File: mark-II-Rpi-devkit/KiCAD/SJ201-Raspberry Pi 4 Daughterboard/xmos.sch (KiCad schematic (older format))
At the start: 55 parts, among them J10 Debug Connector, J8 MIC, Q4 FDV301N, U10 SPK0838HT4H-1, U11 SPK0838HT4H-1, U12 NCP303LSN09, U5 SN74LVC125APWR, U8 XMOS-XVF3510, U9 AT25SF161 16MBIT, X1 SG-210STF 24M

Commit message: SJ201 - Removed CM108b soundcard, added in I2S to Line out, ATTin402. Moved holes in layout. SJ202 - extened length to plug into USB2.0 port
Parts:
- removed R9: 4.7k, Resistor_SMD:R_0402_1005Metric, symbol Device:R_Small
- removed TP28: TestPoint, TestPoint:TestPoint_Pad_D2.0mm, symbol Connector:TestPoint
- C55, C56: MPN CC0402KRX5R6BB105 -> CL05A105KA5NQNC; SKU 302010040 -> (none)
- C65: Link (none) -> https://lcsc.com/product-detail/Multilayer-Ceramic-Capacito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; MPN CC0402KRX7R9BB222 -> 0402B222K500NT; SKU 302010022 -> (none); Vendor (none) -> LCSC
- J10: MPN (none) -> DNP
- J8: LCSC C191721 -> (none); MPN (none) -> DNP
- PWR2: value LED -> LED_RED
- Q4: value FDV301N -> 2N7002; Category Discrete Semiconductor Products -> (none); DK_Datasheet_Link https://media.digikey.com/pdf/Data%20Sheets/Fairchild%20PDF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 -> (none); DK_Detail_Page /product-detail/en/on-semiconductor/FDV301N/FDV301NCT-ND/45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 -> (none); Description MOSFET N-CH 25V 220MA SOT-23 -> MOSFET N TRENCH 60V 115MA 2.5V @ 250UA 7.5 ? @ 500MA,10V SO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; Digi-Key_PN FDV301NCT-ND -> (none); Family Transistors - FETs, MOSFETs - Single -> (none); LCSC C15310 -> C8545; MPN FDV301N -> 2N7002; Manufacturer ON Semiconductor -> (none); Status Active -> (none)
- R34: MPN (none) -> 0402WGF330JTCE
- R5: MPN (none) -> 0402WGF100JTCE
- U10, U11: value SPK0838HT4H-1 -> SPK0641HT4H-1; Digikey 423-1432-1-ND -> 423-1425-1-ND; Link https://www.digikey.com/product-detail/en/knowles/SPK0838HT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 -> https://www.digikey.com/product-detail/en/knowles/SPK0641HT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; MPN SPK0838HT4H-1 -> SPK0641HT4H-1
- U8: MPN XVF3510 -> XVF3510-QF60-C
- U9: MPN AT25SF161 16MBIT -> AT25SF161-SSHD-T
- X1: MPN SG-210STF 24M -> SG-210STF 24.0000ML3
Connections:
- net labels added: GPIO22, GPIO23, GPIO24, GPIO25, SCL_XMOS, SDA_XMOS
- net labels removed: I2C_SCL, I2C_SDA, INT_N, TP5
- wire segments 237 -> 239
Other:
- note added: "Optional Mic:\nSPK0838HT4H-1"
- note removed: "Optional Mic:\nIM69D130"

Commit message: SJ-201 v3, sent to PCB Fab. Removed USB Hub, add in I2S to Line Out
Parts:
- added J15: Output, Connector_PinHeader_1.27mm:PinHeader_1x04_P1.27mm_Vertical_SMD_Pin1Left, symbol Connector_Generic:Conn_01x04
- added R58, R59, R60, R61: 0R DNP, Resistor_SMD:R_0603_1608Metric, symbol Device:R_Small
- C65: Tempo (none) -> C0402C222K5RACTU
- PWR2: Tempo (none) -> 19-217/R6C-AL1M2VY/3T
- Q4: Description MOSFET N TRENCH 60V 115MA 2.5V @ 250UA 7.5 ? @ 500MA,10V SO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 -> N-Channel MOSFET, Enhancement Mode, 60V, 0.115A, 7.5Ω; Manufacturer (none) -> ON Semiconductor
- R32, R34, R35, R36: Tempo (none) -> RC0402FR-0733RL
- R41: Tempo (none) -> RC0402JR-074K7L
- R43, R44, R45, R46: Tempo (none) -> RC0402FR-07100RL
- R5: Tempo (none) -> ERJ-2RKF10R0X
- U9: Digikey 1265-1230-1-ND -> 1265-1278-2-ND; Link https://www.digikey.com/product-detail/en/adesto-technologi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 -> https://www.digikey.com/en/products/detail/adesto-technolog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; MPN AT25SF161-SSHD-T -> AT25SF161-SHD-T
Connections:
- wire segments 239 -> 243
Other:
- note added: "I2S Data out \nfrom XMOS to\nI2S to Lineout IC"
- note removed: "I2S Data from \nUSB Soundcard"
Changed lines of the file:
@@
 Sheet 6 6
 Title ""
-Date "2020-09-26"
-Rev "0.67b"
+Date "2020-10-02"
+Rev "0.67c"
 Comp ""
 Comment1 ""
@@
 F 4 "C25105" H 2150 5150 50  0001 C CNN "LCSC"
 F 5 "0402WGF330JTCE" H 2150 5150 50  0001 C CNN "MPN"
+F 6 "RC0402FR-0733RL" H 2150 5150 50  0001 C CNN "Tempo"
 	1    2150 5150
 	1    0    0    -1
@@
 F 4 "0402WGF330JTCE" H 2225 4350 50  0001 C CNN "MPN"
 F 5 "C25105" H 2225 4350 50  0001 C CNN "LCSC"
+F 6 "RC0402FR-0733RL" H 2225 4350 50  0001 C CNN "Tempo"
 	1    2225 4350
 	0    1    1    0
@@
 F 4 "0402WGF330JTCE" H 2225 4250 50  0001 C CNN "MPN"
 F 5 "C25105" H 2225 4250 50  0001 C CNN "LCSC"
+F 6 "RC0402FR-0733RL" H 2225 4250 50  0001 C CNN "Tempo"
 	1    2225 4250
 	0    1    1    0
@@
 F 4 "0402WGF330JTCE" H 1550 3250 50  0001 C CNN "MPN"
 F 5 "C25105" H 1550 3250 50  0001 C CNN "LCSC"
+F 6 "RC0402FR-0733RL" H 1550 3250 50  0001 C CNN "Tempo"
 	1    1550 3250
 	0    1    1    0
@@
 F 2 "Package_SO:SOIC-8_5.23x5.23mm_P1.27mm" H 7200 2025 50  0001 C CNN
 F 3 "http://ww1.microchip.com/downloads/en/DeviceDoc/Atmel-8707-SEEPROM-AT25010B-020B-040B-Datasheet.pdf" H 7200 2025 50  0001 C CNN
-F 4 "1265-1230-1-ND" H 7200 2025 50  0001 C CNN "Digikey"
-F 5 "AT25SF161-SSHD-T" H 7200 2025 50  0001 C CNN "MPN"
-F 6 "https://www.digikey.com/product-detail/en/adesto-technologies/AT25SF161-SSHD-T/1265-1230-2-ND/6124893" H 7200 2025 50  0001 C CNN "Link"
+F 4 "1265-1278-2-ND" H 7200 2025 50  0001 C CNN "Digikey"
+F 5 "AT25SF161-SHD-T" H 7200 2025 50  0001 C CNN "MPN"
+F 6 "https://www.digikey.com/en/products/detail/adesto-technologies/AT25SF161-SHD-T/6827526" H 7200 2025 50  0001 C CNN "Link"
 F 7 "C93710" H 7200 2025 50  0001 C CNN "LCSC"
 	1    7200 2025
@@
 F 4 "0402WGF4701TCE" H 5125 3450 50  0001 C CNN "MPN"
 F 5 "C25900" H 5125 3450 50  0001 C CNN "LCSC"
+F 6 "RC0402JR-074K7L" H 5125 3450 50  0001 C CNN "Tempo"
 	1    5125 3450
 	-1   0    0    1
@@
 F 4 "0402WGF1000TCE" H 10200 3600 50  0001 C CNN "MPN"
 F 5 "C25076" H 10200 3600 50  0001 C CNN "LCSC"
+F 6 "RC0402FR-07100RL" H 10200 3600 50  0001 C CNN "Tempo"
 	1    10200 3600
 	0    1    1    0
@@
 F 4 "0402WGF1000TCE" H 10200 3700 50  0001 C CNN "MPN"
 F 5 "C25076" H 10200 3700 50  0001 C CNN "LCSC"
+F 6 "RC0402FR-07100RL" H 10200 3700 50  0001 C CNN "Tempo"
 	1    10200 3700
 	0    1    1    0
@@
 F 4 "0402WGF1000TCE" H 10200 4925 50  0001 C CNN "MPN"
 F 5 "C25076" H 10200 4925 50  0001 C CNN "LCSC"
+F 6 "RC0402FR-07100RL" H 10200 4925 50  0001 C CNN "Tempo"
 	1    10200 4925
 	0    1    1    0
@@
 F 4 "0402WGF1000TCE" H 10200 5025 50  0001 C CNN "MPN"
 F 5 "C25076" H 10200 5025 50  0001 C CNN "LCSC"
+F 6 "RC0402FR-07100RL" H 10200 5025 50  0001 C CNN "Tempo"
 	1    10200 5025
 	0    1    1    0
@@
 Text GLabel 4025 1550 2    51   Input ~ 0
 I2S_DATA
-Text Notes 5050 1175 0    63   ~ 0
-I2S Data from \nUSB Soundcard
 $Comp
 L kevin:Ferrite_Bead_Small FB6
@@
 F 8 "" H 3675 8275 60  0001 L CNN "DK_Datasheet_Link"
 F 9 "" H 3675 8375 60  0001 L CNN "DK_Detail_Page"
-F 10 "MOSFET N TRENCH 60V 115MA 2.5V @ 250UA 7.5 ? @ 500MA,10V SOT-23(SOT-23-3) ROHS" H 3675 8475 60  0001 L CNN "Description"
-F 11 "" H 3675 8575 60  0001 L CNN "Manufacturer"
+F 10 "N-Channel MOSFET, Enhancement Mode, 60V, 0.115A, 7.5Ω" H 3675 8475 60  0001 L CNN "Description"
+F 11 "ON Semiconductor" H 3675 8575 60  0001 L CNN "Manufacturer"
 F 12 "" H 3675 8675 60  0001 L CNN "Status"
 F 13 "C8545" H 3475 7475 50  0001 C CNN "LCSC"
@@
 F 6 "https://lcsc.com/product-detail/Others_TOGIALED-TJ-S1608SW6TGLC2R-A5_C192315.html" V 3325 7075 50  0001 C CNN "Link"
 F 7 "304090042" H 3325 7075 50  0001 C CNN "SKU"
+F 8 "19-217/R6C-AL1M2VY/3T" H 3325 7075 50  0001 C CNN "Tempo"
 	1    3325 7075
 	-1   0    0    1
@@
 F 4 "C25077" H 2150 5350 50  0001 C CNN "LCSC"
 F 5 "0402WGF100JTCE" H 2150 5350 50  0001 C CNN "MPN"
+F 6 "ERJ-2RKF10R0X" H 2150 5350 50  0001 C CNN "Tempo"
 	1    2150 5350
 	1    0    0    -1
@@
 F 6 "https://lcsc.com/product-detail/Multilayer-Ceramic-Capacitors-MLCC-SMD-SMT_2-2nF-222-10-50V_C1531.html/?href=jlc-SMT" H 1050 7500 50  0001 C CNN "Link"
 F 7 "LCSC" H 1050 7500 50  0001 C CNN "Vendor"
+F 8 "C0402C222K5RACTU" H 1050 7500 50  0001 C CNN "Tempo"
 	1    1050 7500
 	1    0    0    -1
@@
 Wire Wire Line
 	4025 4500 4225 4500
-Text GLabel 4225 4500 2    51   Input ~ 0
+Text GLabel 4975 4500 2    51   Input ~ 0
 GPIO22
-Text GLabel 4225 4700 2    51   Input ~ 0
+Text GLabel 4975 4700 2    51   Input ~ 0
 GPIO24
-Text GLabel 4225 4800 2    51   Input ~ 0
+Text GLabel 4975 4800 2    51   Input ~ 0
 GPIO25
-Text GLabel 4225 4600 2    51   Input ~ 0
+Text GLabel 4975 4600 2    51   Input ~ 0
 GPIO23
 Wire Wire Line
@@
 Wire Wire Line
 	4025 3050 4725 3050
+$Comp
+L Connector_Generic:Conn_01x04 J15
+U 1 1 5F75C2D9
+P 4775 5125
+F 0 "J15" H 4775 5350 50  0000 C CNN
+F 1 "Output" H 4775 4825 50  0000 C CNN
+F 2 "Connector_PinHeader_1.27mm:PinHeader_1x04_P1.27mm_Vertical_SMD_Pin1Left" H 4775 5125 50  0001 C CNN
+F 3 "~" H 4775 5125 50  0001 C CNN
+F 4 "DNP" H 4775 5125 50  0001 C CNN "MPN"
+	1    4775 5125
+	-1   0    0    -1
+$EndComp
+Text GLabel 4975 5025 2    51   Input ~ 0
+TP1
+Text GLabel 4975 5125 2    51   Input ~ 0
+TP2
+Text GLabel 4975 5225 2    51   Input ~ 0
+TP3
+Text GLabel 4975 5325 2    51   Input ~ 0
+TP4
+Text Notes 4650 1700 0    63   ~ 0
+I2S Data out \nfrom XMOS to\nI2S to Lineout IC
+$Comp
+L Device:R_Small R?
+U 1 1 5F9B65AF
+P 4325 4500
+AR Path="/5EA9C461/5F9B65AF" Ref="R?"  Part="1"
+AR Path="/5EA9C67D/5F9B65AF" Ref="R?"  Part="1"
+AR Path="/5EA9C76D/5F9B65AF" Ref="R58"  Part="1"
+F 0 "R58" V 4275 4275 50  0000 L CNN
+F 1 "0R DNP" V 4375 4600 50  0000 L CNN
+F 2 "Resistor_SMD:R_0603_1608Metric" H 4325 4500 50  0001 C CNN
+F 3 "~" H 4325 4500 50  0001 C CNN
+F 4 "DNP-0603WAF0000T5E" H 4325 4500 50  0001 C CNN "MPN"
+F 5 "C21189-DNP" H 4325 4500 50  0001 C CNN "LCSC"
+	1    4325 4500
+	0    1    1    0
+$EndComp
+$Comp
+L Device:R_Small R?
+U 1 1 5F9E9135
+P 4325 4600
+AR Path="/5EA9C461/5F9E9135" Ref="R?"  Part="1"
+AR Path="/5EA9C67D/5F9E9135" Ref="R?"  Part="1"
+AR Path="/5EA9C76D/5F9E9135" Ref="R59"  Part="1"
+F 0 "R59" V 4275 4375 50  0000 L CNN
+F 1 "0R DNP" V 4375 4700 50  0000 L CNN
+F 2 "Resistor_SMD:R_0603_1608Metric" H 4325 4600 50  0001 C CNN
+F 3 "~" H 4325 4600 50  0001 C CNN
+F 4 "DNP-0603WAF0000T5E" H 4325 4600 50  0001 C CNN "MPN"
+F 5 "C21189-DNP" H 4325 4600 50  0001 C CNN "LCSC"
+	1    4325 4600
+	0    1    1    0
+$EndComp
+$Comp
+L Device:R_Small R?
+U 1 1 5F9E932A
+P 4325 4700
+AR Path="/5EA9C461/5F9E932A" Ref="R?"  Part="1"
+AR Path="/5EA9C67D/5F9E932A" Ref="R?"  Part="1"
+AR Path="/5EA9C76D/5F9E932A" Ref="R60"  Part="1"
+F 0 "R60" V 4275 4475 50  0000 L CNN
+F 1 "0R DNP" V 4375 4800 50  0000 L CNN
+F 2 "Resistor_SMD:R_0603_1608Metric" H 4325 4700 50  0001 C CNN
+F 3 "~" H 4325 4700 50  0001 C CNN
+F 4 "DNP-0603WAF0000T5E" H 4325 4700 50  0001 C CNN "MPN"
+F 5 "C21189-DNP" H 4325 4700 50  0001 C CNN "LCSC"
+	1    4325 4700
+	0    1    1    0
+$EndComp
+$Comp
+L Device:R_Small R?
+U 1 1 5F9E94DF
+P 4325 4800
+AR Path="/5EA9C461/5F9E94DF" Ref="R?"  Part="1"
+AR Path="/5EA9C67D/5F9E94DF" Ref="R?"  Part="1"
+AR Path="/5EA9C76D/5F9E94DF" Ref="R61"  Part="1"
+F 0 "R61" V 4275 4575 50  0000 L CNN
+F 1 "0R DNP" V 4375 4900 50  0000 L CNN
+F 2 "Resistor_SMD:R_0603_1608Metric" H 4325 4800 50  0001 C CNN
+F 3 "~" H 4325 4800 50  0001 C CNN
+F 4 "DNP-0603WAF0000T5E" H 4325 4800 50  0001 C CNN "MPN"
+F 5 "C21189-DNP" H 4325 4800 50  0001 C CNN "LCSC"
+	1    4325 4800
+	0    1    1    0
+$EndComp
+Wire Wire Line
+	4975 4500 4425 4500
+Wire Wire Line
+	4425 4600 4975 4600
+Wire Wire Line
+	4975 4700 4425 4700
+Wire Wire Line
+	4975 4800 4425 4800
 $EndSCHEMATC

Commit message: Rev4 Update - Add in Coral TPU, TAS5806, remove I2S * MAX9744. Change Attiny to Attin1614
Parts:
- removed C65: 2.2NF, Capacitor_SMD:C_0402_1005Metric, symbol Device:C_Small
- removed C66: 1NF, Capacitor_SMD:C_0402_1005Metric, symbol Device:C_Small
- removed J15: Output, Connector_PinHeader_1.27mm:PinHeader_1x04_P1.27mm_Vertical_SMD_Pin1Left, symbol Connector_Generic:Conn_01x04
- removed J8: MIC, Connector_PinHeader_2.54mm:PinHeader_1x03_P2.54mm_Vertical, symbol Connector_Generic:Conn_01x03
- removed PWR2: LED_RED, LED_SMD:LED_0603_1608Metric, symbol Device:LED
- removed Q4: 2N7002, digikey-footprints:SOT-23-3, symbol dk_Transistors-FETs-MOSFETs-Single:FDV301N
- removed R52: 10k, Resistor_SMD:R_0402_1005Metric, symbol Device:R_Small
- removed R53: 330R, Resistor_SMD:R_0402_1005Metric, symbol Device:R_Small
- removed R58, R59, R60, R61: 0R DNP, Resistor_SMD:R_0603_1608Metric, symbol Device:R_Small
- removed U12: NCP303LSN09, Package_TO_SOT_SMD:SOT-23-5, symbol user:NCP303LSN30
- added R22: 330R, Resistor_SMD:R_0402_1005Metric, symbol Device:R_Small
- added R42: 4.7k, Resistor_SMD:R_0402_1005Metric, symbol Device:R_Small
- added TP10, TP11, TP9: TestPoint, TestPoint:TestPoint_Pad_D2.0mm, symbol Connector:TestPoint
- J10: footprint Connector_PinHeader_2.54mm:PinHeader_2x10_P2.54mm_Vertical -> Connector_PinHeader_2.54mm:PinHeader_2x09_P2.54mm_Vertical_SMD; symbol Connector_Generic:Conn_02x10_Odd_Even -> Connector_Generic:Conn_02x09_Odd_Even
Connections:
- net labels added: Boot_Sel, I2S_BCLK_XMOS, I2S_DOUT_XMOS, I2S_LRCK_XMOS, I2S_MCLK_XMOS, SDOUT_I2S_AMP, SPI_CLK, SPI_CSn, XMOS_SendReset
- net labels removed: GPIO22, GPIO23, GPIO24, GPIO25, I2S_BCLK, I2S_DATA, I2S_DOUT, I2S_LRCK, I2S_SCK, SPI_CS_N, TP1, TP2, TP3, TP4
- wire segments 243 -> 220
- no-connect marks 9 -> 15
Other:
- note removed: "I2S Data out \nfrom XMOS to\nI2S to Lineout IC"
- note removed: "Power on RESET"

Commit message: Rev4 Update - fix some wiring, export for printing Rev 4
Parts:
- D20: LCSC C179724-DNP -> C179724
- U9: LCSC C93710 -> C93711
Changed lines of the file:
@@
 Sheet 6 7
 Title "XMOS"
-Date "2020-11-18"
-Rev "4.01"
+Date "2020-11-22"
+Rev "Rev4 - 0.03"
 Comp "Mycroft"
-Comment1 "SJ201 r4.01"
+Comment1 "SJ-201-R4"
 Comment2 ""
 Comment3 ""
@@
 F 5 "AT25SF161-SHD-T" H 7200 2025 50  0001 C CNN "MPN"
 F 6 "https://www.digikey.com/en/products/detail/adesto-technologies/AT25SF161-SHD-T/6827526" H 7200 2025 50  0001 C CNN "Link"
-F 7 "C93710" H 7200 2025 50  0001 C CNN "LCSC"
+F 7 "C93711" H 7200 2025 50  0001 C CNN "LCSC"
 	1    7200 2025
 	1    0    0    -1
@@
 F 3 "http://www.diodes.com/_files/datasheets/ds11005.pdf" H 6630 6075 50  0001 C CNN
 F 4 "BAT54ALT1G" H 6750 6075 50  0001 C CNN "MPN"
-F 5 "C179724-DNP" H 6750 6075 50  0001 C CNN "LCSC"
+F 5 "C179724" H 6750 6075 50  0001 C CNN "LCSC"
 	1    6750 6075
 	0    1    1    0

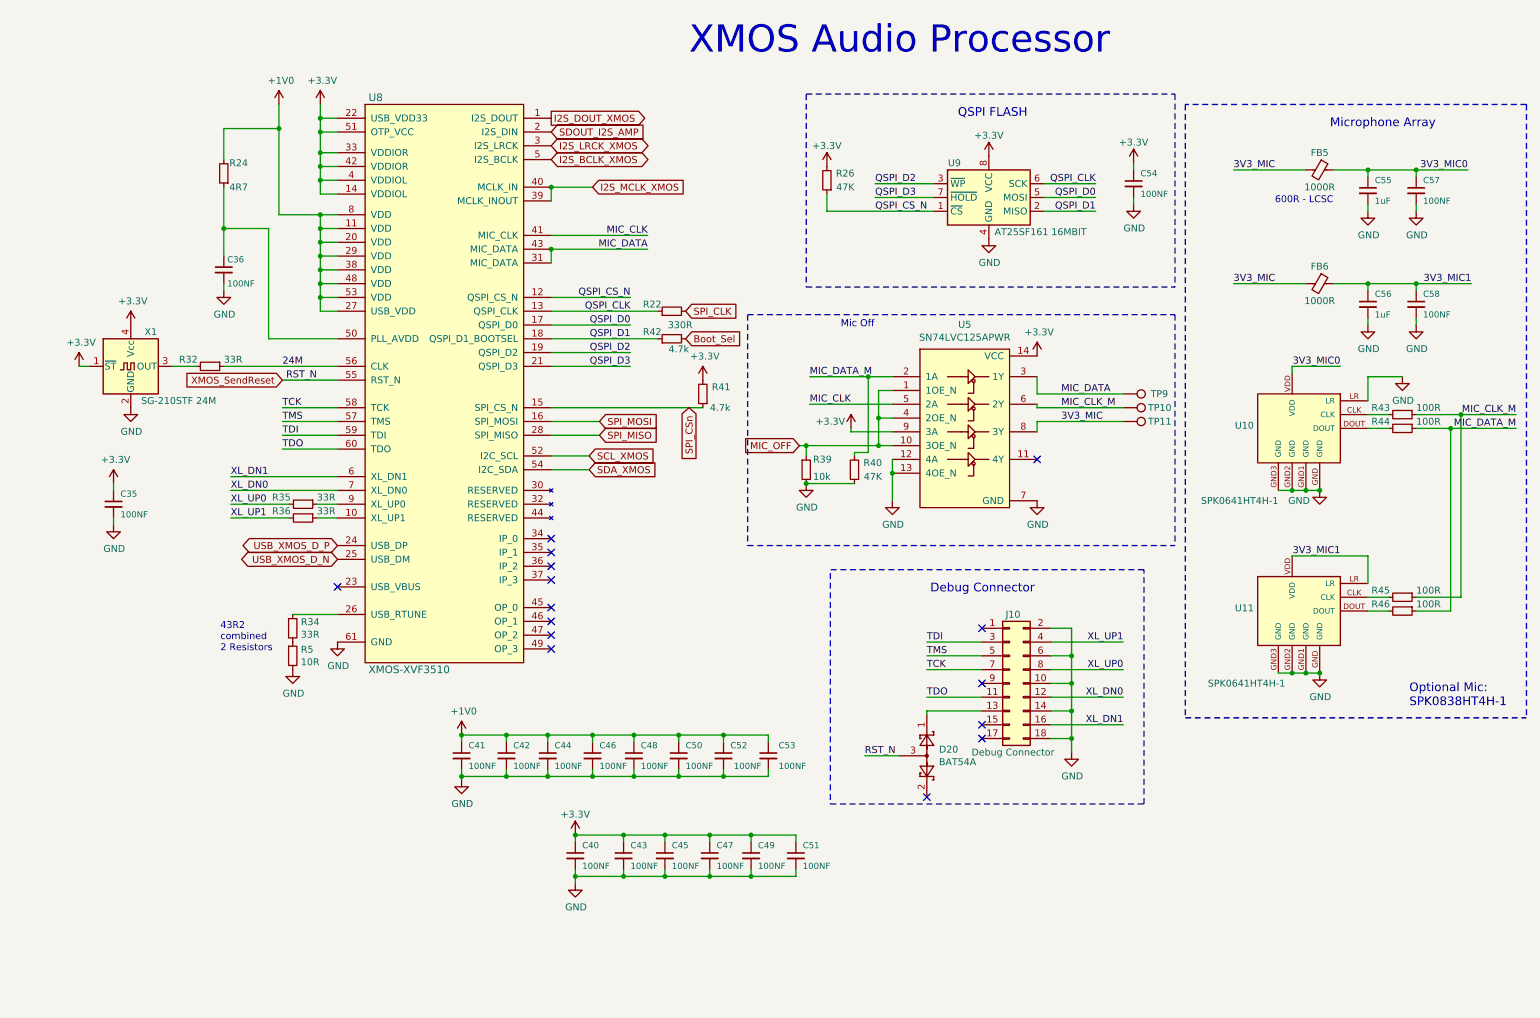
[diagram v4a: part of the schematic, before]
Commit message: SJ-201-R6 for FAB - removed buffer IC
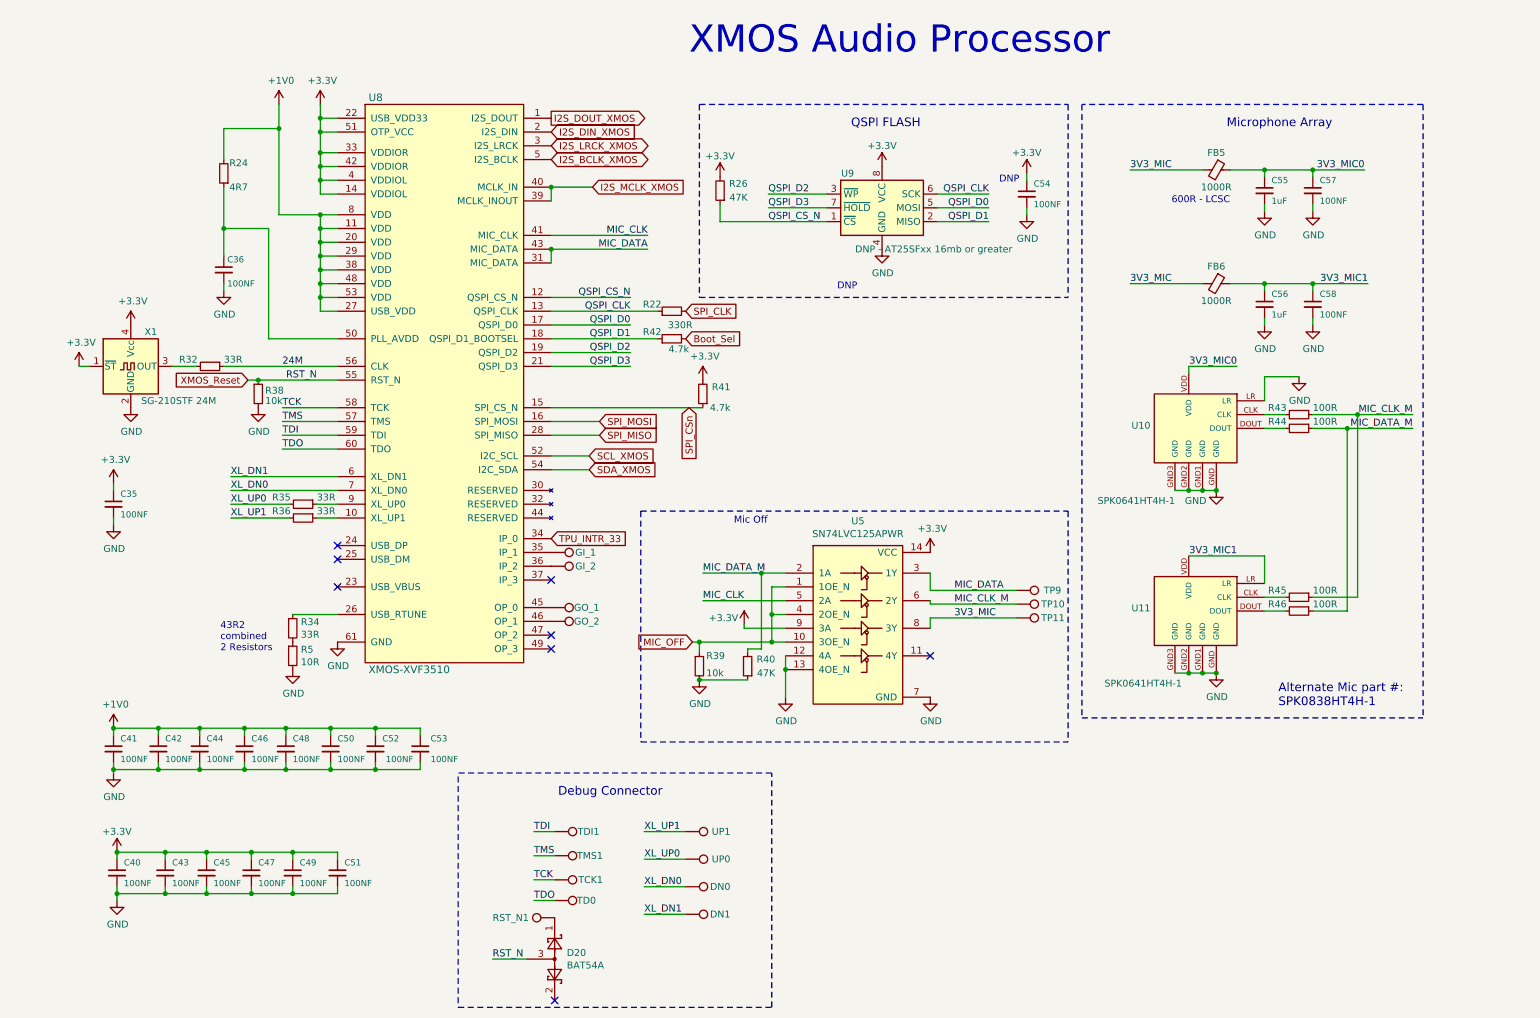
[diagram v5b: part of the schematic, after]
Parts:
- removed J10: Debug Connector, Connector_PinHeader_2.54mm:PinHeader_2x09_P2.54mm_Vertical_SMD, symbol Connector_Generic:Conn_02x09_Odd_Even
- added DN0, DN1, TCK1, TD0, TDI1, TMS1, UP0, UP1: TestPoint, TestPoint:TestPoint_Pad_D1.0mm, symbol Connector:TestPoint
- added GI_1, GI_2, GO_1, GO_2, RST_N1: TestPoint, TestPoint:TestPoint_Pad_D2.0mm, symbol Connector:TestPoint
- added R38: 10k, Resistor_SMD:R_0402_1005Metric, symbol Device:R_Small
- R26: MPN RC0402JR-0747KL -> 0402WGF4702TCE; SKU 301010005 -> (none)
- R40: SKU 301010005 -> (none)
- U9: value AT25SF161 16MBIT -> DNP - AT25SFxx 16mb or greater; Digikey 1265-1278-2-ND -> (none); LCSC C93711 -> C93710-DNP; MPN AT25SF161-SHD-T -> AT25SF161-SHD-T-DNP
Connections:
- net GND: now also R38.2
- net TCK: now also TCK1.1
- net TDI: now also TDI1.1
- net TDO: now also TD0.1
- net TMS: now also TMS1.1
- net XL_DN0: now also DN0.1
- net XL_DN1: now also DN1.1
- net XL_UP0: now also UP0.1
- net XL_UP1: now also UP1.1
- net TPU_INTR_33: now reaches U8.34 (IP_0)
- net at U8.35 (IP_1): now also GI_1.1
- net at U8.36 (IP_2): now also GI_2.1
- net at U8.45 (OP_0): now also GO_1.1
- net at U8.46 (OP_1): now also GO_2.1
- net at D20.1: now also RST_N1.1
- net SDOUT_I2S_AMP renamed I2S_DIN_XMOS
- net USB_XMOS_D_N: no longer names the net of U8.25 (USB_DM)
- net USB_XMOS_D_P: no longer names the net of U8.24 (USB_DP)
- net XMOS_SendReset renamed XMOS_Reset
- net XMOS_Reset: now also R38.1
- no-connect marks 15 -> 8
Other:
- note added: "Alternate Mic part #:\nSPK0838HT4H-1"
- note added: "DNP"
- note removed: "Optional Mic:\nSPK0838HT4H-1"
- moved on the sheet: C40, C41, C42, C43, C44, C45, C46, C47, C48, C49, C50, C51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

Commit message: Updated files for R6 v2
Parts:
- U8: footprint user:QFN-60-1EP_7x7mm_P0.4mm_EP5.6x5.6mm-HandSolder -> user:QFN-60-1EP_7x7mm_P0.4mm_EP5.6x5.6mm
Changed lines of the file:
@@
 Sheet 6 8
 Title "XMOS"
-Date "2020-12-30"
-Rev "Rev5 - v1"
+Date "2021-01-27"
+Rev "Rev6 - v2"
 Comp "Mycroft AI"
 Comment1 "SJ-201-R6"
@@
 F 0 "U8" H 2700 1400 55  0000 L CNN
 F 1 "XMOS-XVF3510" H 2700 -2750 55  0000 L CNN
-F 2 "user:QFN-60-1EP_7x7mm_P0.4mm_EP5.6x5.6mm-HandSolder" H 3275 1350 55  0001 C CNN
+F 2 "user:QFN-60-1EP_7x7mm_P0.4mm_EP5.6x5.6mm" H 3275 1350 55  0001 C CNN
 F 3 "" H 3275 1350 55  0001 C CNN
 F 4 "XVF3510-QF60-C" H 3275 1350 50  0001 C CNN "MPN"
